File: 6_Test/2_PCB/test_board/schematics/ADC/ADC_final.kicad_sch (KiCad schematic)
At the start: 19 parts, among them J1 BNC1, J2 BNC2, J3 TSW-107-07-F-D, J4 TSW-107-07-F-D

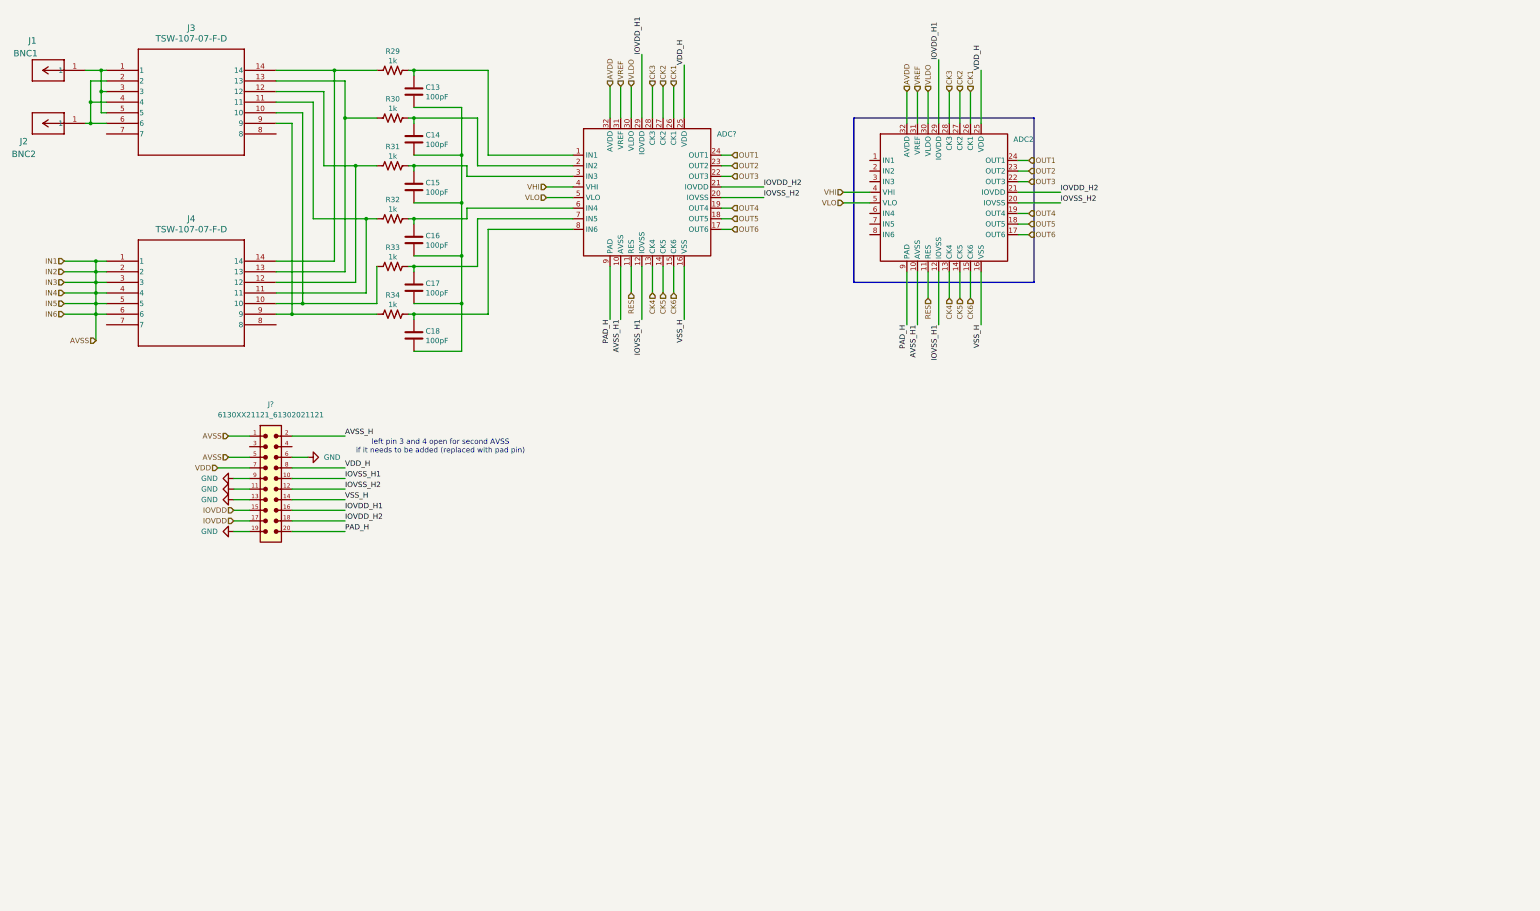
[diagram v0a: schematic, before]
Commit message: made changes with accordance to feedback. Remvoed excess files.
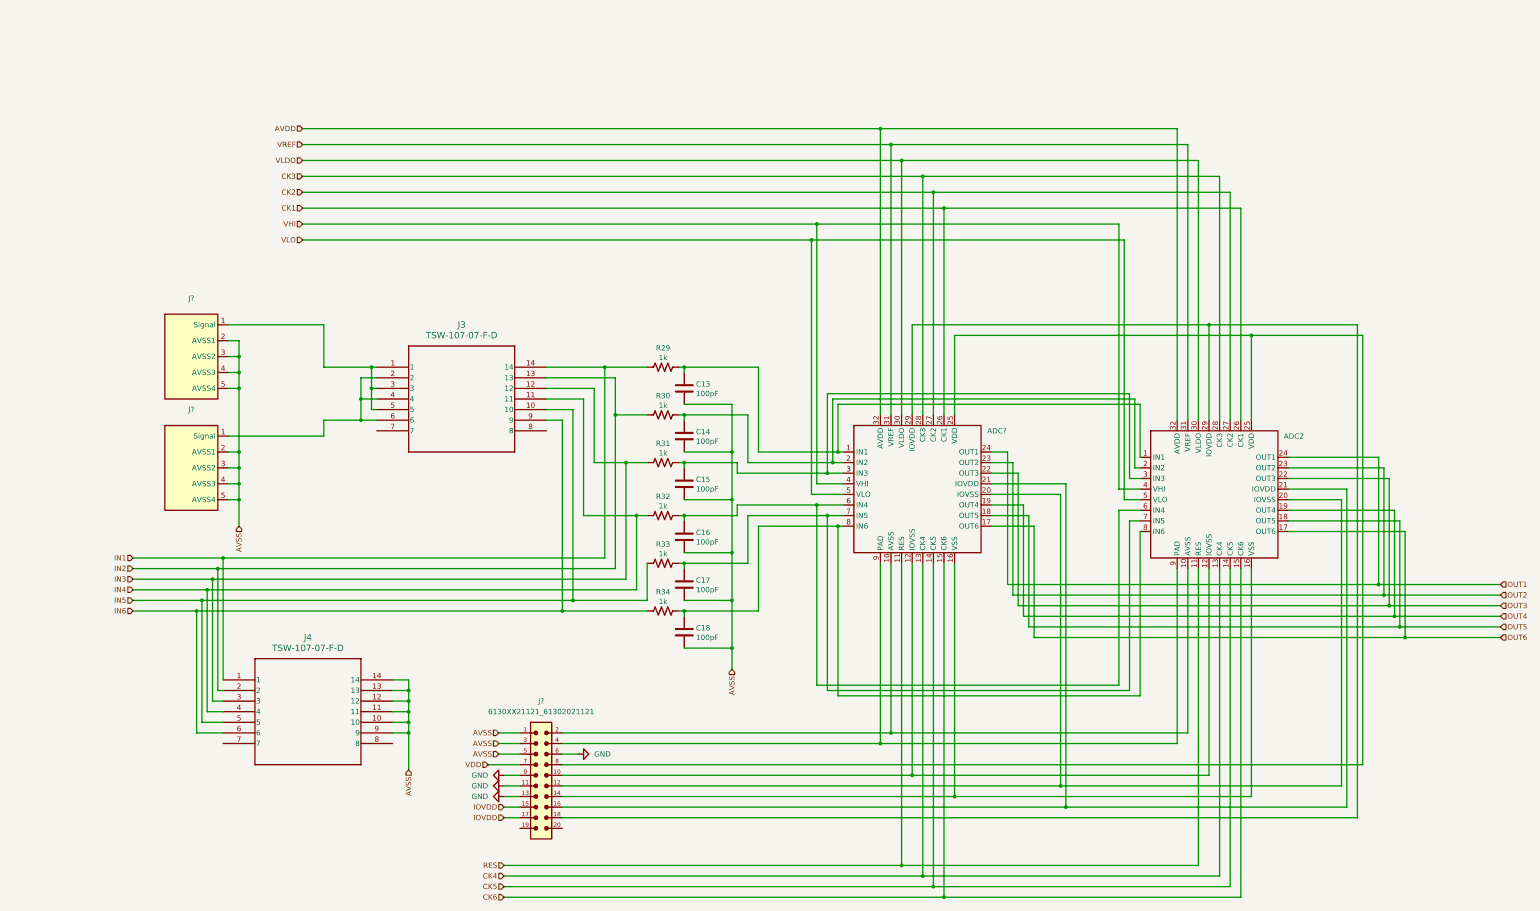
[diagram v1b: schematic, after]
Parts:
- removed J1: BNC1, CONN_1274571-1_TYCO, symbol bnc_mini:1274571-1
- removed J2: BNC2, CONN_1274571-1_TYCO, symbol bnc_mini:1274571-1
- added J? (x2): ~, symbol bnc_mini_gnd:bnc_mini_gnd
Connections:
- net AVSS_H1 is gone; now on an unnamed net: ADC2.10 (AVSS), ADC?.10 (AVSS)
- net AVSS: now also C13.2, C14.2, C15.2, C16.2, C17.2, C18.2, J4.10, J4.11, J4.12, J4.13, J4.14, J4.9, J?.3, J?.2 (AVSS1), J?.2 (AVSS1), J?.3 (AVSS2), J?.3 (AVSS2), J?.4 (AVSS3), J?.4 (AVSS3), J?.5 (AVSS4), J?.5 (AVSS4); no longer J4.1, J4.2, J4.3, J4.4, J4.5, J4.6
- net GND: no longer J?.19
- net IN5: now reaches J3.10, R33.1
- net IN5: now also J4.5; no longer J4.10
- net at ADC?.7 (IN5), C17.1, R33.2: now also ADC2.7 (IN5)
- net IN2: now reaches J3.13, R30.1
- net IN2: now also J4.2; no longer J4.13
- net at ADC?.2 (IN2), C14.1, R30.2: now also ADC2.2 (IN2)
- net IN4: now reaches J3.11, R32.1
- net IN4: now also J4.4; no longer J4.11
- net at ADC?.6 (IN4), C16.1, R32.2: now also ADC2.6 (IN4)
- net at ADC?.8 (IN6), C18.1, R34.2: now also ADC2.8 (IN6)
- net at ADC?.1 (IN1), C13.1, R29.2: now also ADC2.1 (IN1)
- net at J3.1, J3.3, J3.5: now also J?.1 (Signal)
- net IN3: now reaches J3.12, R31.1
- net IN3: now also J4.3; no longer J4.12
- net IN1: now reaches J3.14, R29.1
- net IN1: now also J4.1; no longer J4.14
- net at J3.2, J3.4, J3.6: now also J?.1 (Signal)
- net IN6: now reaches J3.9, R34.1
- net IN6: now also J4.6; no longer J4.9
- net at J?.4: now also ADC2.9 (PAD), ADC?.9 (PAD)
- net at ADC?.3 (IN3), C15.1, R31.2: now also ADC2.3 (IN3)
- net AVSS_H: no longer names the net of J?.2
- net IOVDD_H1: no longer names the net of ADC2.29 (IOVDD), ADC?.29 (IOVDD)
- net IOVDD_H1: now also J?.18; no longer J?.16
- net IOVDD_H2: no longer names the net of ADC2.21 (IOVDD), ADC?.21 (IOVDD)
- net IOVDD_H2: now also J?.16; no longer J?.18
- net IOVSS_H1: no longer names the net of ADC2.12 (IOVSS), ADC?.12 (IOVSS), J?.10
- net IOVSS_H2: no longer names the net of ADC2.20 (IOVSS), ADC?.20 (IOVSS), J?.12
- removed net PAD_H: ADC2.9 (PAD), ADC?.9 (PAD), J?.20
- net VDD_H: no longer names the net of ADC2.25 (VDD), ADC?.25 (VDD), J?.8
- net VSS_H: no longer names the net of ADC2.16 (VSS), ADC?.16 (VSS), J?.14
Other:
- note removed: "left pin 3 and 4 open for second AVSS if it needs to be added (replaced with pad pin)"
- title: (none) -> ADC
- moved on the sheet: ADC2, ADC?, C13, C14, C15, C16, C17, C18, J3, J4, J?, R29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
